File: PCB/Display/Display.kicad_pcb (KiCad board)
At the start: 2 copper layers, 44.5 x 67 mm, 30 parts, among them J1 DC, J2 USB-C, M1 OLED1.5-RGB, U1 L86-M33, U2 ESP32-PICO-MINI-02, U3 FT231XQ, U4 LMR16006+FB, U5 QR

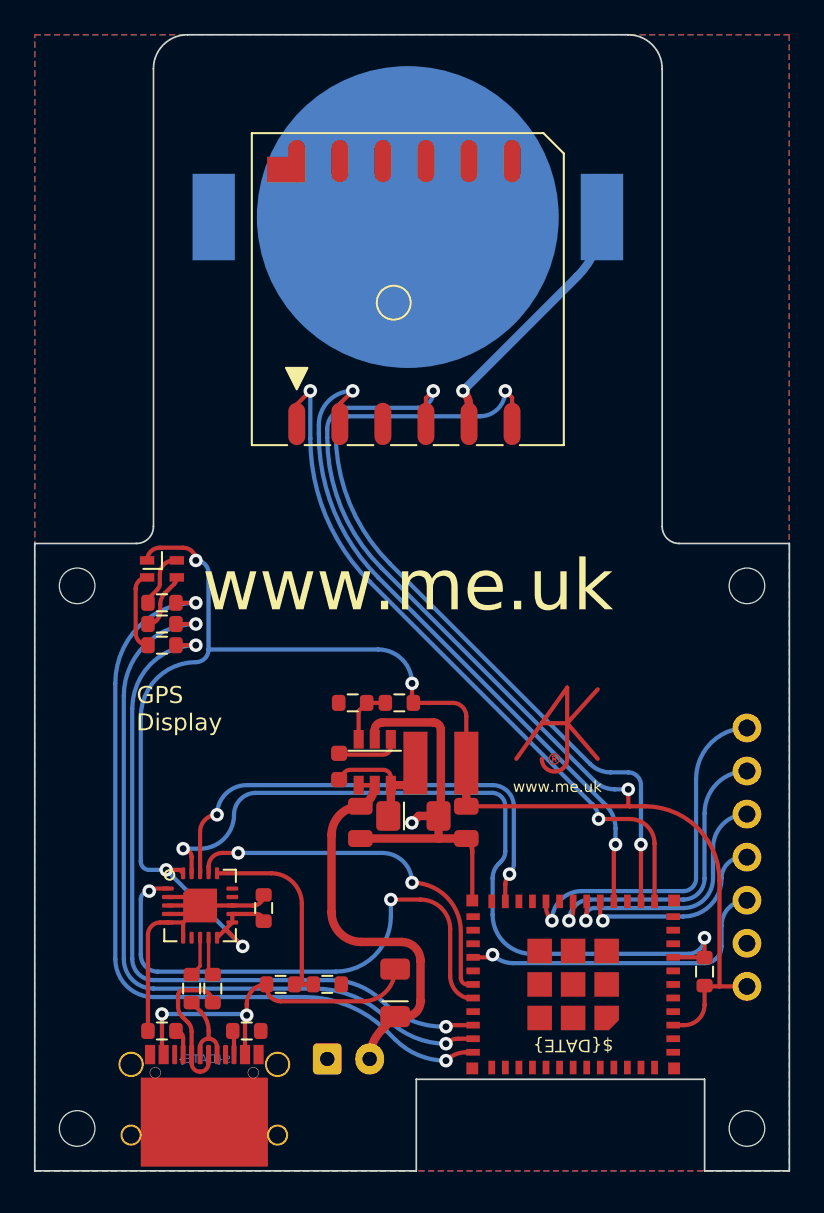
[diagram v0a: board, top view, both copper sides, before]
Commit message: Started update on display.
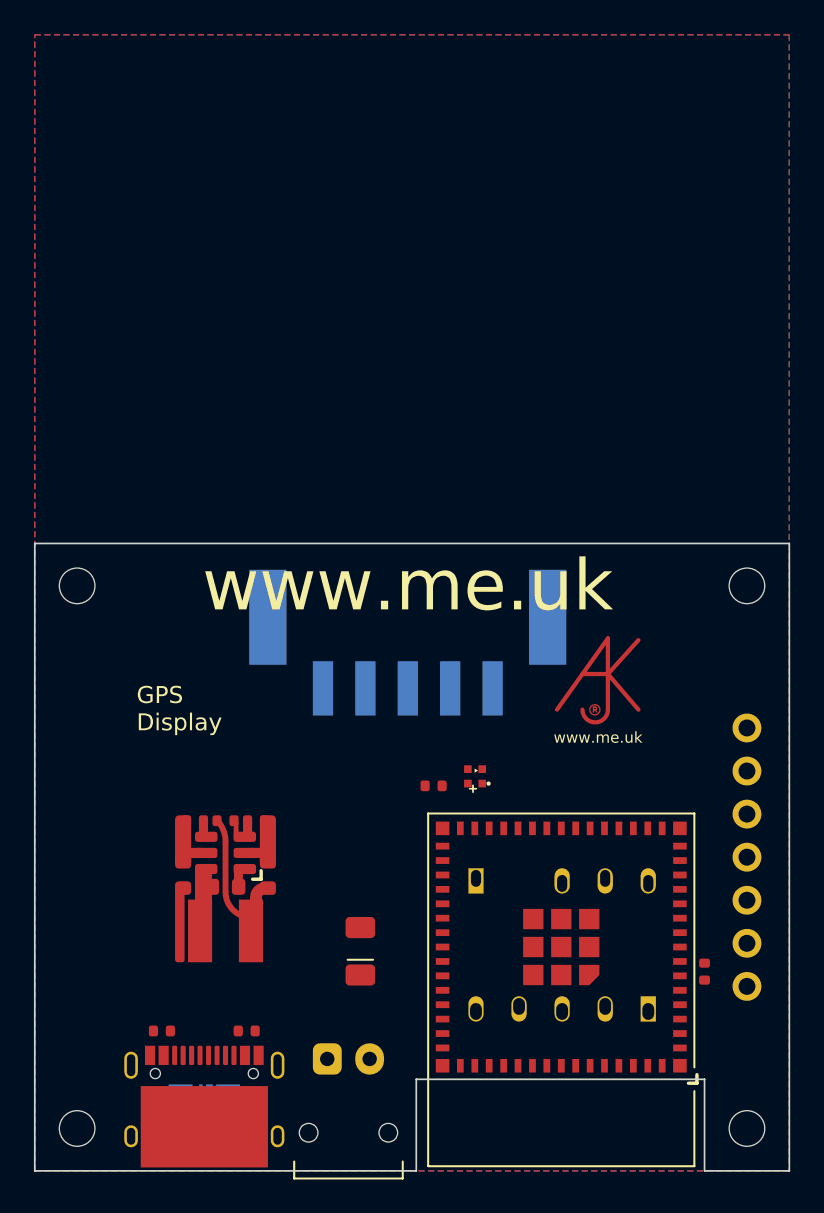
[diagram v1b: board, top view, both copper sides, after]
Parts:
- removed BT1: Battery_Cell, RevK:Battery-Holder-2032
- removed C1: 0.1uF, RevK:C_0603
- removed C2: 0.1uF, RevK:Hidden
- removed C3: 2.2uF, RevK:Hidden
- removed C4: 10uF, RevK:Hidden
- removed D2: LED_RGBA, RevK:LED-RGB-1.6x1.6
- removed D3: Schottky, RevK:Hidden
- removed L1: 6.8uH, RevK:Hidden
- removed R10: 2K, RevK:R_0603
- removed R11: 220R, RevK:R_0603
- removed R12: 30k 1% or NF, RevK:R_0603
- removed R4, R5: 27R, RevK:R_0603
- removed R6: 4k7, RevK:R_0603
- removed R7: 10k, RevK:R_0603
- removed R8: 100k 1% or 0R, RevK:R_0603
- removed R9: 680R, RevK:R_0603
- removed U3: FT231XQ, RevK:QFN-20-1EP_4x4mm_P0.5mm_EP2.5x2.5mm
- removed U4: LMR16006+FB, RevK:RegulatorBlockFB
- added C5: 1uF, RevK:C_0402, F.Cu at (101.5, 129.3)
- added C6: 10uF 50V, RevK:C_0603_, F.Cu at (97.2, 119.9)
- added C7: 10uF 6.3V, RevK:C_0603_, F.Cu at (97.2, 121.9)
- added C8: 100nF, RevK:C_0603_, F.Cu at (97.2, 123.8)
- added D4: XL-1010RGBC-WS2812B, RevK:SMD1010, F.Cu at (104.0, 128.7)
- added J3: Conn_01x05, RevK:PTSM-HH-5-RA-SMD, B.Cu at (100.0, 118.2)
- added J4: Shelly, RevK:Shelly, B.Cu at (109.1, 142.4)
- added J5: USB-PROG, RevK:USB-PROG, B.Cu at (109.1, 134.9)
- added L2: 10uH, RevK:L_4x4_, F.Cu at (98.4, 127.3)
- added R13: 124k, RevK:R_0402_, F.Cu at (99.9, 119.9)
- added R14: 40k2, RevK:R_0402_, F.Cu at (99.9, 121.7)
- added R15: 1M, RevK:R_0402_, F.Cu at (99.9, 123.6)
- J1: value DC -> POWER; footprint RevK:Molex_MiniSPOX_H2RA -> RevK:PTSM-HH1-2-RA
- J2: value USB-C -> USB-C-Socket-V; footprint RevK:USC16-TR-Round -> RevK:USB-C-Socket-H
- R1: value 10k -> 10K; footprint RevK:R_0603 -> RevK:R_0402
- R2, R3: footprint RevK:R_0603 -> RevK:R_0402
- U1: value L86-M33 -> ESP32-S3-MINI-1; footprint RevK:L86-M33 -> RevK:ESP32-S3-MINI-1
- U2: value ESP32-PICO-MINI-02 -> MD8942; footprint RevK:ESP32-PICO-MINI-02 -> RevK:SOT-23-6-MD8942
- moved U1 39.8 mm to (109.0, 138.8), turned to 180 degrees
- moved U2 21.9 mm to (89.2, 133.2), turned to 0 degrees
- moved J2 4.35 mm to (88.0, 147.7)
- moved Logo2 3.76 mm to (111.8, 122.7)
- moved D1 3.19 mm to (97.2, 139.1)
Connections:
- J2 pad A6: Net-(J2-PadA6) -> D+
- J2 pad A7: Net-(J2-PadA7) -> D-
- J2 pad B6: Net-(J2-PadA6) -> D+
- J2 pad B7: Net-(J2-PadA7) -> D-
- M1 pad 4: OLED-SCLK -> OLED-SCK
- M1 pad 5: OLED-CS0 -> OLED-CS
- R1 pad 2: EN -> Net-(U1-EN)
- U1 pad 1: GPSRX -> GND
- U1 pad 12: GND -> unconnected-(U1-GPIO8-Pad12)
- U1 pad 2: GPSTX -> GND
- U1 pad 3: GND -> +3V3
- U1 pad 4: +3V3 -> Net-(J4-0)
- U1 pad 5: Net-(BT1-Pad1) -> unconnected-(U1-GPIO1-Pad5)
- U1 pad 6: TICK -> unconnected-(U1-GPIO2-Pad6)
- U2 pad 1: GND -> unconnected-(U2-Pad1)
- U2 pad 3: +3V3 -> unconnected-(U2-Pad3)
- U2 pad 5: unconnected-(U2-Pad5) -> DC
- U2 pad 7: unconnected-(U2-Pad7) -> GND
- U2 pad 8: EN -> +3V3
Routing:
- net +3V3: track 127.9 -> 0.00 mm, vias 6 -> 0
- net TICK: track 49.2 -> 0.00 mm, vias 2 -> 0
- net R: track 48.1 -> 0.00 mm, vias 2 -> 0
- net EN: track 46.8 -> 0.00 mm, vias 2 -> 0
- net G: track 45.6 -> 0.00 mm, vias 2 -> 0
- net B: track 43.1 -> 0.00 mm, vias 2 -> 0
- net GPSRX: track 41.5 -> 0.00 mm, vias 2 -> 0
- net GPSTX: track 40.0 -> 0.00 mm, vias 2 -> 0
- net O: track 32.4 -> 0.00 mm, vias 2 -> 0
- net BOOT: track 28.8 -> 0.00 mm, vias 2 -> 0
- net GND: track 26.5 -> 0.00 mm, vias 1 -> 0
- net DC: track 22.2 -> 0.00 mm
- net I: track 21.8 -> 0.00 mm, vias 2 -> 0
- net OLED-RST: track 21.5 -> 0.00 mm, vias 1 -> 0
- net VBUS: track 21.5 -> 0.00 mm, vias 2 -> 0
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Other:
- board size 44.5 x 67 mm -> 44.5 x 37 mm
- board text removed: "13"
- board text removed: "14"
- board text removed: "26"
- board text removed: "27"
- board text removed: "3.3"
- board text removed: "8"
- board text removed: "DC 4V-60V"
- board text removed: "LED: 21/22/19 GPSTICK: 33 GPSRX: 32 GPSTX: 25"
- board text removed: "⏚"

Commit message: SD
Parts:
- added J6: DM3AT-SF-PEJM5, Connector_Card:microSD_HC_Hirose_DM3AT-SF-PEJM5, B.Cu at (87.0, 133.7)
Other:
- board text removed: "GPS Display"
- board text removed: "www.me.uk"
